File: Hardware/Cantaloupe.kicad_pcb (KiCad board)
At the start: 2 copper layers, 277.1 x 113 mm, 172 parts, among them J1 USB_C_Receptacle_PD, J2 Bat, J3 OLED, J4 USB_C_Receptacle_PD, J5 Bat, J6 OLED, SW1 MX, SW10 MX, SW11 MX, SW12 MX, SW13 MX, SW14 MX, SW15 MX, SW16 MX, SW17 MX, SW18 MX, SW19 MX, SW2 MX, SW20 MX, SW21 MX, SW22 MX, SW23 MX, SW24 MX, SW25 MX, SW26 MX, SW27 MX, SW28 MX, SW29 MX, SW3 MX, SW30 MX, SW31 5_Way_Tactile_Switch, SW32 Rotary_Encoder_Switch, SW33 5_Way_Tactile_Switch_R, SW34 Reset, SW35 MX, SW36 MX, SW37 MX, SW38 MX, SW39 MX, SW4 MX, SW40 MX, SW41 MX, SW42 MX, SW43 MX, SW44 MX, SW45 MX, SW46 MX, SW47 MX, SW48 MX, SW49 MX, SW5 MX, SW50 MX, SW51 MX, SW52 MX, SW53 MX, SW54 MX, SW55 MX, SW56 MX, SW57 MX, SW58 MX, SW59 MX, SW6 MX, SW60 MX, SW61 MX, SW62 MX, SW63 MX, SW65 MX, SW66 Rotary_Encoder_Switch, SW67 Reset, SW7 MX, SW8 MX, SW9 MX, U1 ProMicro, U2 ProMicro

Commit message: Proper case files and gerbers
Added an STL file for a rudimentary 3D-printed case for the Cantaloupe as well as DXF and Gerber files for a plate.
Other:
- board text added: "Cantaloupe Keyboard Left Hand Side V1.0 Designed By Aria"
- board text added: "Cantaloupe Keyboard Right Hand Side V1.0 Designed By Aria"
- board text removed: "Cantaloupe Keyboard Left Hand Side V2.1 Designed By Aria"
- board text removed: "Cantaloupe Keyboard Right Hand Side V2.1 Designed By Aria"

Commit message: Interconnect changed to C-168688
Changed interconnect footprint to USB C-168688 due to lack of widespread availability of previous part.
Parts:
- J1, J4: footprint Cantaloupe:USB-C-PowerOnly -> Cantaloupe:USB-C-C168688
- R1: value 4.7k -> 10k
- R2: renamed from R4; value 4.7k -> 10k
- moved J4 0.73 mm to (69.1, 113.6)
- moved J1 0.72 mm to (348.1, 113.6)
- renumbered SW32 to SW31, SW31 to SW32, SW34 to SW33, SW35 to SW34, SW36 to SW35, SW37 to SW36, SW38 to SW37, SW39 to SW38, SW40 to SW39, SW41 to SW40, SW42 to SW41, SW43 to SW42, SW44 to SW43, SW45 to SW44, SW46 to SW45, SW47 to SW46, SW48 to SW47, SW49 to SW48, SW50 to SW49, SW51 to SW50, SW52 to SW51, SW53 to SW52, SW58 to SW53, SW63 to SW58, SW65 to SW63, SW66 to SW64, SW33 to SW65, SW67 to SW66
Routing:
- net DATA_R: track 47.7 -> 50.3 mm
- net DATA: track 46.5 -> 49.1 mm
- net VCC: track 73.4 -> 72.3 mm
- net GND3: track 247.1 -> 246.0 mm
- net GND1: track 99.1 -> 98.1 mm
- net VDD: track 65.4 -> 66.4 mm

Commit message: Updated to V1.1
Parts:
- removed D63, D64, D65, D66, D67, D68, D69, D70: D, Diode_SMD:D_SOD-123
- removed H1, H10, H2, H3, H4, H5, H6, H7, H8, H9: MountingHole, MountingHole:MountingHole_2.2mm_M2_Pad
- removed H11 (x2), H12 (x2), H13 (x2), H14 (x2), H15 (x2): Breakaway, Cantaloupe:Breakaway_Tabs
- removed R1, R2: 10k, Resistor_SMD:R_0603_1608Metric_Pad1.05x0.95mm_HandSolder
- removed the REF** at (343.6, 94.9)
- removed the REF** at (327.6, 94.9)
- removed the REF** at (89.5, 94.9)
- removed the REF** at (73.5, 94.9)
- added J7: BAT_CON_TOG, Cantaloupe:Battery_Solder_Points, F.Cu at (309.2, 33.8)
- added J8: BAT_CON_R, Cantaloupe:Battery_Solder_Points, F.Cu at (77.6, 39.1)
- added J9: BAT_CON, Cantaloupe:Battery_Solder_Points, F.Cu at (334.6, 39.1)
- added REF**: MountingHole_2.2mm_M2_Pad, MountingHole:MountingHole_2.2mm_M2_Pad, F.Cu at (174.6, 60.3)
- added REF**: Breakaway_Tabs, Custom Parts:Breakaway_Tabs, F.Cu at (193.9, 127.0)
- added REF**: Breakaway_Tabs, Custom Parts:Breakaway_Tabs, F.Cu at (193.9, 88.9)
- added REF**: Breakaway_Tabs, Custom Parts:Breakaway_Tabs, F.Cu at (193.9, 69.8)
- added REF**: Breakaway_Tabs, Custom Parts:Breakaway_Tabs, F.Cu at (193.9, 108.0)
- added REF**: LiPo_501235, Custom Parts:LiPo_501235, F.Cu at (317.4, 92.9)
- added REF**: MountingHole_2.2mm_M2_Pad, MountingHole:MountingHole_2.2mm_M2_Pad, F.Cu at (330.4, 72.5)
- added REF**: MountingHole_2.2mm_M2_Pad, MountingHole:MountingHole_2.2mm_M2_Pad, F.Cu at (314.4, 72.5)
- added REF**: MountingHole_2.2mm_M2_Pad, MountingHole:MountingHole_2.2mm_M2_Pad, F.Cu at (309.4, 121.5)
- added REF**: MountingHole_2.2mm_M2_Pad, MountingHole:MountingHole_2.2mm_M2_Pad, F.Cu at (270.3, 112.7)
- added REF**: MountingHole_2.2mm_M2_Pad, MountingHole:MountingHole_2.2mm_M2_Pad, F.Cu at (289.4, 57.1)
- added REF**: MountingHole_2.2mm_M2_Pad, MountingHole:MountingHole_2.2mm_M2_Pad, F.Cu at (98.4, 57.1)
- added REF**: MountingHole_2.2mm_M2_Pad, MountingHole:MountingHole_2.2mm_M2_Pad, F.Cu at (213.2, 117.5)
- added REF**: MountingHole_2.2mm_M2_Pad, MountingHole:MountingHole_2.2mm_M2_Pad, F.Cu at (213.2, 60.3)
- added REF**: MountingHole_2.2mm_M2_Pad, MountingHole:MountingHole_2.2mm_M2_Pad, F.Cu at (117.5, 112.7)
- added REF**: MountingHole_2.2mm_M2_Pad, MountingHole:MountingHole_2.2mm_M2_Pad, F.Cu at (174.6, 117.5)
- added REF**: MountingHole_2.2mm_M2_Pad, MountingHole:MountingHole_2.2mm_M2_Pad, F.Cu at (78.4, 121.5)
- added REF**: MountingHole_2.2mm_M2_Pad, MountingHole:MountingHole_2.2mm_M2_Pad, F.Cu at (73.4, 72.3)
- added REF**: MountingHole_2.2mm_M2_Pad, MountingHole:MountingHole_2.2mm_M2_Pad, F.Cu at (57.4, 72.3)
- added REF**: LiPo_501235, Custom Parts:LiPo_501235, F.Cu at (70.4, 92.9)
- added REF**: Breakaway_Tabs, Custom Parts:Breakaway_Tabs, F.Cu at (193.9, 50.8)
- added SW67: BAT_TOG, Cantaloupe:Switch_MSK-22D18, F.Cu at (303.2, 35.1)
- added SW68: BAT_TOG_R, Cantaloupe:Switch_MSK-22D18, F.Cu at (84.6, 35.1)
- J1, J4: value USB_C_Receptacle_PD -> OLED; footprint Cantaloupe:USB-C-C168688 -> Cantaloupe:PinHeader_1x04_P2.54mm_Vertical_No_Silk; moved to F.Cu
- J2: value Bat -> Interconnect; footprint Cantaloupe:Battery_Solder_Points -> Cantaloupe:USB-C_C168688; moved to B.Cu
- J3: value OLED -> ICSP; footprint Cantaloupe:PinHeader_1x04_P2.54mm_Vertical_No_Silk -> Connector_PinHeader_2.54mm:PinHeader_2x03_P2.54mm_Vertical; moved to B.Cu
- J5: value Bat -> Interconnect_R; footprint Cantaloupe:Battery_Solder_Points -> Cantaloupe:USB-C_C168688; moved to B.Cu
- J6: value OLED -> ICSP_R; footprint Cantaloupe:PinHeader_1x04_P2.54mm_Vertical_No_Silk -> Connector_PinHeader_2.54mm:PinHeader_2x03_P2.54mm_Vertical; moved to B.Cu
- SW31, SW64: value Rotary_Encoder_Switch -> MX; footprint Rotary_Encoder:RotaryEncoder_Alps_EC11E-Switch_Vertical_H20mm -> Cantaloupe:CherryMX_Hotswap_SMK
- SW32: value 5_Way_Tactile_Switch -> Encoder; footprint Cantaloupe:5-way_Tactile_Switch -> Rotary_Encoder:RotaryEncoder_Alps_EC11E-Switch_Vertical_H20mm
- SW65: value 5_Way_Tactile_Switch_R -> Encoder_R; footprint Cantaloupe:5-way_Tactile_Switch -> Rotary_Encoder:RotaryEncoder_Alps_EC11E-Switch_Vertical_H20mm
- moved SW34 144.1 mm to (63.5, 120.3), turned to 30 degrees
- moved D32 143.2 mm to (70.3, 116.3), turned to 120 degrees
- moved SW35 134.2 mm to (73.0, 136.8), turned to 30 degrees
- moved D33 133.3 mm to (79.9, 132.8), turned to 120 degrees
- moved SW36 125.3 mm to (88.9, 49.2)
- moved SW38 125.3 mm to (88.9, 87.3)
- moved SW37 125.3 mm to (88.9, 68.3)
- moved D36 124.8 mm to (96.8, 87.3)
- moved D35 124.8 mm to (96.8, 68.3)
- moved D34 124.8 mm to (96.8, 49.2)
- moved SW63 105.1 mm to (184.2, 108.0), turned to 0 degrees
- moved SW64 103.6 mm to (184.2, 127.0), turned to 0 degrees
- moved D61 102.7 mm to (192.1, 108.0), turned to 90 degrees
- moved D62 98.5 mm to (192.1, 127.0), turned to 90 degrees
- moved D58 98.0 mm to (192.1, 50.8)
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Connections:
- D30 pad 1: ROW1 -> ROW4
- D32 pad 1: ROW1_R -> ROW4_R
- D33 pad 1: ROW2_R -> ROW5_R
- D34 pad 1: ROW3_R -> ROW1_R
- D35 pad 1: ROW4_R -> ROW2_R
- D36 pad 1: ROW5_R -> ROW3_R
- D37 pad 1: ROW1_R -> ROW4_R
- D38 pad 1: ROW2_R -> ROW5_R
- D39 pad 1: ROW3_R -> ROW1_R
- D40 pad 1: ROW4_R -> ROW2_R
- D41 pad 1: ROW5_R -> ROW3_R
- D42 pad 1: ROW1_R -> ROW4_R
- D43 pad 1: ROW2_R -> ROW5_R
- D44 pad 1: ROW3_R -> ROW1_R
- D45 pad 1: ROW4_R -> ROW2_R
- D46 pad 1: ROW5_R -> ROW3_R
- D47 pad 1: ROW1_R -> ROW4_R
- D48 pad 1: ROW2_R -> ROW1_R
- D49 pad 1: ROW3_R -> ROW2_R
- D50 pad 1: ROW4_R -> ROW3_R
- D51 pad 1: ROW1_R -> ROW4_R
- D52 pad 1: ROW2_R -> ROW5_R
- D53 pad 1: ROW3_R -> ROW1_R
- D54 pad 1: ROW4_R -> ROW2_R
- D55 pad 1: ROW5_R -> ROW3_R
- D56 pad 1: ROW1_R -> ROW4_R
- D57 pad 1: ROW2_R -> ROW5_R
- D58 pad 1: ROW3_R -> ROW1_R
- D59 pad 1: ROW4_R -> ROW2_R
- D60 pad 1: ROW5_R -> ROW3_R
- D61 pad 1: ROW1_R -> ROW4_R
- J3 pad 1: GND1 -> ROW4
- J3 pad 3: SCL -> ROW5
- J3 pad 4: SDA -> ROW3
- J6 pad 1: GND3 -> COL5_R
- J6 pad 3: SCL_R -> COL4_R
- J6 pad 4: SDA_R -> COL6_R
- SW24 pad 1: COL4 -> COL5
- SW29 pad 1: COL5 -> COL6
- SW30 pad 1: COL6 -> COL7
- SW30 pad 2: Net-(D31-Pad2) -> Net-(D30-Pad2)
- SW33 pad 2: GND2 -> GND1
- SW34 pad 1: COL1_R -> COL7_R
- SW35 pad 1: COL1_R -> COL7_R
- SW36 pad 1: COL1_R -> COL6_R
- SW37 pad 1: COL1_R -> COL6_R
- SW38 pad 1: COL1_R -> COL6_R
- SW39 pad 1: COL2_R -> COL6_R
- SW40 pad 1: COL2_R -> COL6_R
- SW41 pad 1: COL2_R -> COL5_R
- SW42 pad 1: COL2_R -> COL5_R
- SW43 pad 1: COL2_R -> COL5_R
- SW44 pad 1: COL3_R -> COL5_R
- SW45 pad 1: COL3_R -> COL5_R
- SW46 pad 1: COL3_R -> COL4_R
- SW47 pad 1: COL3_R -> COL4_R
- SW48 pad 1: COL3_R -> COL4_R
- SW50 pad 1: COL4_R -> COL3_R
- SW51 pad 1: COL4_R -> COL3_R
- SW52 pad 1: COL4_R -> COL3_R
- SW53 pad 1: COL4_R -> COL3_R
- SW53 pad 2: Net-(D55-Pad2) -> Net-(D51-Pad2)
- SW54 pad 1: COL5_R -> COL3_R
- SW54 pad 2: Net-(D51-Pad2) -> Net-(D52-Pad2)
- SW55 pad 1: COL5_R -> COL2_R
- SW55 pad 2: Net-(D52-Pad2) -> Net-(D53-Pad2)
- SW56 pad 1: COL5_R -> COL2_R
- SW56 pad 2: Net-(D53-Pad2) -> Net-(D54-Pad2)
- SW57 pad 1: COL5_R -> COL2_R
- SW57 pad 2: Net-(D54-Pad2) -> Net-(D55-Pad2)
- SW58 pad 1: COL5_R -> COL2_R
- SW58 pad 2: Net-(D60-Pad2) -> Net-(D56-Pad2)
- SW59 pad 1: COL6_R -> COL2_R
- SW59 pad 2: Net-(D56-Pad2) -> Net-(D57-Pad2)
- SW60 pad 1: COL6_R -> COL1_R
- SW60 pad 2: Net-(D57-Pad2) -> Net-(D58-Pad2)
- SW61 pad 1: COL6_R -> COL1_R
- SW61 pad 2: Net-(D58-Pad2) -> Net-(D59-Pad2)
- SW62 pad 1: COL6_R -> COL1_R
- SW62 pad 2: Net-(D59-Pad2) -> Net-(D60-Pad2)
- SW63 pad 1: COL6_R -> COL1_R
- SW63 pad 2: Net-(D62-Pad2) -> Net-(D61-Pad2)
- U1 pad 1: ROTA -> ROW1
- U1 pad 10: DATA -> COL4
- U1 pad 11: COL4 -> COL5
- U1 pad 12: COL5 -> COL6
- U1 pad 13: ROW1 -> ROW2
- U1 pad 14: ROW2 -> ROW3
- U1 pad 15: COL6 -> ROW4
- U1 pad 16: ROW3 -> ROW5
- U1 pad 17: ROW4 -> ROT_B
- U1 pad 18: ROW5 -> ROT_A
- U1 pad 2: ROTB -> DATA
- U1 pad 24: Net-(J2-Pad2) -> Net-(J9-Pad2)
- U1 pad 3: GND2 -> Net-(U1-Pad3)
- U1 pad 4: GND2 -> Net-(U1-Pad4)
- U2 pad 1: ROW5_R -> COL7_R
- U2 pad 10: DATA_R -> ROW4_R
- U2 pad 11: Net-(U2-Pad11) -> ROW3_R
- U2 pad 12: COL7_R -> ROW2_R
- U2 pad 13: ROTA_R -> Net-(U2-Pad13)
- U2 pad 14: ROTB_R -> COL6_R
- U2 pad 15: COL6_R -> COL5_R
- U2 pad 16: COL5_R -> COL4_R
- U2 pad 17: COL4_R -> COL3_R
- U2 pad 18: COL3_R -> COL2_R
- U2 pad 19: COL2_R -> COL1_R
- U2 pad 2: ROW4_R -> DATA_R
- U2 pad 20: COL1_R -> ROW1_R
- U2 pad 24: Net-(J5-Pad2) -> RAW_R
- U2 pad 7: ROW3_R -> ROT_A_R
- U2 pad 8: ROW2_R -> ROT_B_R
- U2 pad 9: ROW1_R -> ROW5_R
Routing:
- net GND2: track 145.9 -> 0.00 mm, vias 3 -> 0
- net ROT_A_R: track 0.00 -> 104.4 mm
- net ROT_B: track 0.00 -> 103.3 mm
- net ROTA: track 99.2 -> 0.00 mm
- net ROT_A: track 0.00 -> 98.9 mm
- net ROT_B_R: track 0.00 -> 96.2 mm
- net ROTB: track 87.4 -> 0.00 mm
- net GND3: track 246.0 -> 169.3 mm, vias 2 -> 0
- net COL7_R: track 90.3 -> 166.1 mm, vias 2 -> 0
- net ROTB_R: track 75.2 -> 0.00 mm, vias 1 -> 0
- net ROW1_R: track 217.8 -> 148.8 mm, vias 3 -> 0
- net ROTA_R: track 65.0 -> 0.00 mm, vias 1 -> 0
- net GND1: track 98.1 -> 159.8 mm
- net ROW4: track 188.0 -> 247.9 mm, vias 0 -> 3
- net ROW1: track 198.0 -> 138.6 mm, vias 3 -> 0
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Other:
- board size 277.1 x 113 mm -> 284.6 x 117 mm
- net class Battery added: clearance 0.2, trace_width 1, via_dia 0.7, via_drill 0.35
- board text added: "Cantaloupe Left V1.1 Aria"
- board text added: "Cantaloupe Right V1.1 Aria"
- board text added: "JLCJLCJLCJLC"
- board text added: "OLED"
- board text removed: "Cantaloupe Keyboard Left Hand Side V1.0 Designed By Aria"
- board text removed: "Cantaloupe Keyboard Right Hand Side V1.0 Designed By Aria"
- board text removed: "JLCJLCJLC"

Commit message: Increased gap between halves
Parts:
- removed the REF** at (174.6, 60.3)
- removed the REF** at (193.9, 127.0)
- removed the REF** at (193.9, 88.9)
- removed the REF** at (193.9, 69.8)
- removed the REF** at (193.9, 108.0)
- removed the REF** at (309.4, 121.5)
- removed the REF** at (270.3, 112.7)
- removed the REF** at (289.4, 57.1)
- removed the REF** at (98.4, 57.1)
- removed the REF** at (213.2, 117.5)
- removed the REF** at (213.2, 60.3)
- removed the REF** at (117.5, 112.7)
- removed the REF** at (174.6, 117.5)
- removed the REF** at (193.9, 50.8)
- added REF**: Breakaway_Tabs, Custom Parts:Breakaway_Tabs, F.Cu at (196.8, 88.8)
- added REF**: Breakaway_Tabs, Custom Parts:Breakaway_Tabs, F.Cu at (193.7, 69.8)
- added REF**: MountingHole_2.2mm_M2_Pad, MountingHole:MountingHole_2.2mm_M2_Pad, F.Cu at (174.6, 60.3)
- added REF**: MountingHole_2.2mm_M2_Pad, MountingHole:MountingHole_2.2mm_M2_Pad, F.Cu at (98.4, 57.1)
- added REF**: MountingHole_2.2mm_M2_Pad, MountingHole:MountingHole_2.2mm_M2_Pad, F.Cu at (117.5, 112.6)
- added REF**: MountingHole_2.2mm_M2_Pad, MountingHole:MountingHole_2.2mm_M2_Pad, F.Cu at (174.6, 117.4)
- added REF**: Breakaway_Tabs, Custom Parts:Breakaway_Tabs, F.Cu at (193.7, 107.9)
- added REF**: MountingHole_2.2mm_M2_Pad, MountingHole:MountingHole_2.2mm_M2_Pad, F.Cu at (312.2, 121.5)
- added REF**: MountingHole_2.2mm_M2_Pad, MountingHole:MountingHole_2.2mm_M2_Pad, F.Cu at (273.1, 112.6)
- added REF**: MountingHole_2.2mm_M2_Pad, MountingHole:MountingHole_2.2mm_M2_Pad, F.Cu at (292.1, 57.1)
- added REF**: MountingHole_2.2mm_M2_Pad, MountingHole:MountingHole_2.2mm_M2_Pad, F.Cu at (215.9, 117.4)
- added REF**: MountingHole_2.2mm_M2_Pad, MountingHole:MountingHole_2.2mm_M2_Pad, F.Cu at (215.9, 60.3)
- added REF**: Breakaway_Tabs, Custom Parts:Breakaway_Tabs, F.Cu at (196.8, 126.9)
- added REF**: Breakaway_Tabs, Custom Parts:Breakaway_Tabs, F.Cu at (196.8, 107.9)
- added REF**: Breakaway_Tabs, Custom Parts:Breakaway_Tabs, F.Cu at (193.7, 126.9)
- added REF**: Breakaway_Tabs, Custom Parts:Breakaway_Tabs, F.Cu at (193.7, 88.8)
- added REF**: Breakaway_Tabs, Custom Parts:Breakaway_Tabs, F.Cu at (196.8, 50.7)
- added REF**: Breakaway_Tabs, Custom Parts:Breakaway_Tabs, F.Cu at (193.7, 50.7)
- added REF**: Breakaway_Tabs, Custom Parts:Breakaway_Tabs, F.Cu at (196.8, 69.8)
- moved J3 2.74 mm to (337.0, 104.1)
- moved D1 2.74 mm to (214.3, 50.7)
- moved D10 2.74 mm to (233.4, 126.9)
- moved D2 2.74 mm to (214.3, 69.8)
- moved D20 2.74 mm to (290.5, 46.0)
- moved D21 2.74 mm to (290.5, 65.0)
- moved D22 2.74 mm to (290.5, 84.1)
- moved D23 2.74 mm to (290.5, 103.1)
- moved D24 2.74 mm to (284.2, 126.9)
- moved D25 2.74 mm to (309.6, 49.1)
- moved D26 2.74 mm to (309.6, 68.2)
- moved D27 2.74 mm to (309.6, 87.2)
- moved D28 2.74 mm to (309.6, 106.3)
- moved D29 2.74 mm to (305.0, 130.9)
- moved D3 2.74 mm to (214.3, 88.8)
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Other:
- board size 284.6 x 117 mm -> 287.3 x 117 mm

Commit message: Better photo, reorganized footprints, minor fixes to circuit
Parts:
- removed the D32 at (70.3, 116.2)
- removed the D33 at (79.9, 132.7)
- removed the D38 at (100.6, 127.3)
- removed the SW30 at (327.1, 120.2)
- removed the SW34 at (63.5, 120.2)
- added D56: D, Diode_SMD:D_SOD-123, B.Cu at (80.6, 134.0)
- added D57: D, Diode_SMD:D_SOD-123, B.Cu at (101.1, 128.5)
- added D62: D, Diode_SMD:D_SOD-123, B.Cu at (71.1, 117.5)
- added SW32: 5_Way, Cantaloupe:Switch_5-way-tactile, F.Cu at (327.1, 120.2)
- added SW66: 5_Way_R, Cantaloupe:Switch_5-way-tactile, F.Cu at (63.5, 120.2)
- SW1, SW23, SW29, SW42, SW64: footprint Cantaloupe:CherryMX_Hotswap_SMK -> Cantaloupe:MX-1U-Hotswap
- SW10: renamed from SW17; footprint Cantaloupe:CherryMX_Hotswap_SMK -> Cantaloupe:MX-1U-Hotswap
- SW11: renamed from SW21; footprint Cantaloupe:CherryMX_Hotswap_SMK -> Cantaloupe:MX-1U-Hotswap
- SW12: renamed from SW26; footprint Cantaloupe:CherryMX_Hotswap_SMK -> Cantaloupe:MX-1U-Hotswap
- SW13: renamed from SW3; footprint Cantaloupe:CherryMX_Hotswap_SMK -> Cantaloupe:MX-1U-Hotswap
- SW14: renamed from SW8; footprint Cantaloupe:CherryMX_Hotswap_SMK -> Cantaloupe:MX-1U-Hotswap
- SW15: renamed from SW13; footprint Cantaloupe:CherryMX_Hotswap_SMK -> Cantaloupe:MX-1U-Hotswap
- SW16: renamed from SW18; footprint Cantaloupe:CherryMX_Hotswap_SMK -> Cantaloupe:MX-1U-Hotswap
- SW17: renamed from SW22; footprint Cantaloupe:CherryMX_Hotswap_SMK -> Cantaloupe:MX-1U-Hotswap
- SW18: renamed from SW27; footprint Cantaloupe:CherryMX_Hotswap_SMK -> Cantaloupe:MX-1U-Hotswap
- SW19: renamed from SW4; footprint Cantaloupe:CherryMX_Hotswap_SMK -> Cantaloupe:MX-1U-Hotswap
- SW2: renamed from SW6; footprint Cantaloupe:CherryMX_Hotswap_SMK -> Cantaloupe:MX-1U-Hotswap
- SW20: renamed from SW9; footprint Cantaloupe:CherryMX_Hotswap_SMK -> Cantaloupe:MX-1U-Hotswap
- SW21: renamed from SW14; footprint Cantaloupe:CherryMX_Hotswap_SMK -> Cantaloupe:MX-1U-Hotswap
- SW22: renamed from SW19; footprint Cantaloupe:CherryMX_Hotswap_SMK -> Cantaloupe:MX-1U-Hotswap
- SW24: renamed from SW28; footprint Cantaloupe:CherryMX_Hotswap_SMK -> Cantaloupe:MX-1U-Hotswap
- SW25: renamed from SW5; footprint Cantaloupe:CherryMX_Hotswap_SMK -> Cantaloupe:MX-1U-Hotswap
- SW26: renamed from SW10; footprint Cantaloupe:CherryMX_Hotswap_SMK -> Cantaloupe:MX-1U-Hotswap
- SW27: renamed from SW15; footprint Cantaloupe:CherryMX_Hotswap_SMK -> Cantaloupe:MX-1U-Hotswap
- SW28: renamed from SW24; footprint Cantaloupe:CherryMX_Hotswap_SMK -> Cantaloupe:MX-1U-Hotswap
- SW3: renamed from SW11; footprint Cantaloupe:CherryMX_Hotswap_SMK -> Cantaloupe:MX-1U-Hotswap
- SW30: renamed from SW31; footprint Cantaloupe:CherryMX_Hotswap_SMK -> Cantaloupe:MX-1U-Hotswap
- SW35: renamed from SW36; footprint Cantaloupe:CherryMX_Hotswap_SMK -> Cantaloupe:MX-1U-Hotswap
- SW36: renamed from SW41; footprint Cantaloupe:CherryMX_Hotswap_SMK -> Cantaloupe:MX-1U-Hotswap
- SW37: renamed from SW46; footprint Cantaloupe:CherryMX_Hotswap_SMK -> Cantaloupe:MX-1U-Hotswap
- SW38: renamed from SW50; footprint Cantaloupe:CherryMX_Hotswap_SMK -> Cantaloupe:MX-1U-Hotswap
- SW39: renamed from SW55; footprint Cantaloupe:CherryMX_Hotswap_SMK -> Cantaloupe:MX-1U-Hotswap
- SW4: renamed from SW16; footprint Cantaloupe:CherryMX_Hotswap_SMK -> Cantaloupe:MX-1U-Hotswap
- SW40: renamed from SW60; footprint Cantaloupe:CherryMX_Hotswap_SMK -> Cantaloupe:MX-1U-Hotswap
- SW41: renamed from SW37; footprint Cantaloupe:CherryMX_Hotswap_SMK -> Cantaloupe:MX-1U-Hotswap
- SW43: renamed from SW47; footprint Cantaloupe:CherryMX_Hotswap_SMK -> Cantaloupe:MX-1U-Hotswap
- SW44: renamed from SW51; footprint Cantaloupe:CherryMX_Hotswap_SMK -> Cantaloupe:MX-1U-Hotswap
- SW45: renamed from SW56; footprint Cantaloupe:CherryMX_Hotswap_SMK -> Cantaloupe:MX-1U-Hotswap
- SW46: renamed from SW61; footprint Cantaloupe:CherryMX_Hotswap_SMK -> Cantaloupe:MX-1U-Hotswap
- SW47: renamed from SW38; footprint Cantaloupe:CherryMX_Hotswap_SMK -> Cantaloupe:MX-1U-Hotswap
- SW48: renamed from SW43; footprint Cantaloupe:CherryMX_Hotswap_SMK -> Cantaloupe:MX-1U-Hotswap
- SW49: renamed from SW48; footprint Cantaloupe:CherryMX_Hotswap_SMK -> Cantaloupe:MX-1U-Hotswap
- SW5: renamed from SW20; footprint Cantaloupe:CherryMX_Hotswap_SMK -> Cantaloupe:MX-1U-Hotswap
- SW50: renamed from SW52; footprint Cantaloupe:CherryMX_Hotswap_SMK -> Cantaloupe:MX-1U-Hotswap
- SW51: renamed from SW57; footprint Cantaloupe:CherryMX_Hotswap_SMK -> Cantaloupe:MX-1U-Hotswap
- SW52: renamed from SW62; footprint Cantaloupe:CherryMX_Hotswap_SMK -> Cantaloupe:MX-1U-Hotswap
- SW53: renamed from SW39; footprint Cantaloupe:CherryMX_Hotswap_SMK -> Cantaloupe:MX-1U-Hotswap
- SW54: renamed from SW44; footprint Cantaloupe:CherryMX_Hotswap_SMK -> Cantaloupe:MX-1U-Hotswap
- SW55: renamed from SW49; footprint Cantaloupe:CherryMX_Hotswap_SMK -> Cantaloupe:MX-1U-Hotswap
- SW56: renamed from SW53; footprint Cantaloupe:CherryMX_Hotswap_SMK -> Cantaloupe:MX-1U-Hotswap
- SW57: renamed from SW58; footprint Cantaloupe:CherryMX_Hotswap_SMK -> Cantaloupe:MX-1U-Hotswap
- SW58: renamed from SW63; footprint Cantaloupe:CherryMX_Hotswap_SMK -> Cantaloupe:MX-1U-Hotswap
- SW59: renamed from SW35; footprint Cantaloupe:CherryMX_Hotswap_SMK -> Cantaloupe:MX-1U-Hotswap
- SW6: renamed from SW25; footprint Cantaloupe:CherryMX_Hotswap_SMK -> Cantaloupe:MX-1U-Hotswap
- SW60: renamed from SW40; footprint Cantaloupe:CherryMX_Hotswap_SMK -> Cantaloupe:MX-1U-Hotswap
- SW61: renamed from SW45; footprint Cantaloupe:CherryMX_Hotswap_SMK -> Cantaloupe:MX-1U-Hotswap
- SW62: renamed from SW54; footprint Cantaloupe:CherryMX_Hotswap_SMK -> Cantaloupe:MX-1U-Hotswap
- SW63: renamed from SW59; footprint Cantaloupe:CherryMX_Hotswap_SMK -> Cantaloupe:MX-1U-Hotswap
- SW7: renamed from SW2; footprint Cantaloupe:CherryMX_Hotswap_SMK -> Cantaloupe:MX-1U-Hotswap
- SW8: renamed from SW7; footprint Cantaloupe:CherryMX_Hotswap_SMK -> Cantaloupe:MX-1U-Hotswap
- SW9: renamed from SW12; footprint Cantaloupe:CherryMX_Hotswap_SMK -> Cantaloupe:MX-1U-Hotswap
- moved D30 20.6 mm to (323.7, 142.0)
- moved D31 17.6 mm to (333.2, 125.5), turned to 240 degrees
- moved G1 2.47 mm to (261.1, 119.8)
- moved D29 1.72 mm to (304.7, 132.6)
- moved D1 1.50 mm to (214.3, 52.2)
- moved D10 1.50 mm to (271.5, 62.6)
- moved D11 1.50 mm to (290.5, 66.5)
- moved D12 1.50 mm to (309.6, 69.7)
- moved D13 1.50 mm to (214.3, 90.3)
- moved D14 1.50 mm to (233.4, 90.3)
- moved D15 1.50 mm to (252.4, 85.6)
- moved D16 1.50 mm to (271.5, 81.6)
- moved D17 1.50 mm to (290.5, 85.6)
- moved D18 1.50 mm to (309.6, 88.7)
- moved D19 1.50 mm to (214.3, 109.4)
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- renumbered D17 to D10, D21 to D11, D26 to D12, D3 to D13, D8 to D14, D13 to D15, D18 to D16, D22 to D17, D27 to D18, D4 to D19, D6 to D2, D9 to D20, D14 to D21, D19 to D22, D28 to D24, D5 to D25, D10 to D26, D15 to D27, D24 to D28, D11 to D3, D34 to D32, D39 to D33, D44 to D34, D48 to D35, D53 to D36, D58 to D37, D35 to D38, D40 to D39, D16 to D4, D45 to D40, D49 to D41, D54 to D42, D59 to D43, D36 to D44, D41 to D45, D50 to D47, D55 to D48, D60 to D49, D20 to D5, D37 to D50, D42 to D51, D47 to D52, D51 to D53, D56 to D54, D61 to D55, D43 to D58, D52 to D59, D25 to D6, D57 to D60, D62 to D61, D2 to D7, D7 to D8, D12 to D9, J9 to J1, J1 to J2, J2 to J3, J3 to J4, J7 to J5, J4 to J6, J5 to J7, J6 to J8, J8 to J9, SW33 to SW31, SW67 to SW33, SW32 to SW34, SW66 to SW65, SW65 to SW67
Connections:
- D1 pad 1: ROW1 -> ROW0
- D10 pad 1: ROW2 -> ROW1
- D11 pad 1: ROW2 -> ROW1
- D12 pad 1: ROW2 -> ROW1
- D13 pad 1: ROW3 -> ROW2
- D14 pad 1: ROW3 -> ROW2
- D15 pad 1: ROW3 -> ROW2
- D16 pad 1: ROW3 -> ROW2
- D17 pad 1: ROW3 -> ROW2
- D18 pad 1: ROW3 -> ROW2
- D19 pad 1: ROW4 -> ROW3
- D2 pad 1: ROW1 -> ROW0
- D20 pad 1: ROW4 -> ROW3
- D21 pad 1: ROW4 -> ROW3
- D22 pad 1: ROW4 -> ROW3
- D23 pad 1: ROW4 -> ROW3
- D24 pad 1: ROW4 -> ROW3
- D25 pad 1: ROW5 -> ROW4
- D26 pad 1: ROW5 -> ROW4
- D27 pad 1: ROW5 -> ROW4
- D28 pad 1: ROW5 -> ROW4
- D29 pad 1: ROW5 -> ROW4
- D3 pad 1: ROW1 -> ROW0
- D31 pad 1: ROW5 -> Net-(D31-Pad1)
- D31 pad 2: Net-(D31-Pad2) -> PERIPH
- D32 pad 1: ROW1_R -> ROW0_R
- D33 pad 1: ROW1_R -> ROW0_R
- D34 pad 1: ROW1_R -> ROW0_R
- D35 pad 1: ROW1_R -> ROW0_R
- D36 pad 1: ROW1_R -> ROW0_R
- D37 pad 1: ROW1_R -> ROW0_R
- D38 pad 1: ROW2_R -> ROW1_R
- D39 pad 1: ROW2_R -> ROW1_R
- D4 pad 1: ROW1 -> ROW0
- D40 pad 1: ROW2_R -> ROW1_R
- D41 pad 1: ROW2_R -> ROW1_R
- D42 pad 1: ROW2_R -> ROW1_R
- D43 pad 1: ROW2_R -> ROW1_R
- D44 pad 1: ROW3_R -> ROW2_R
- D45 pad 1: ROW3_R -> ROW2_R
- D46 pad 1: ROW3_R -> ROW2_R
- D47 pad 1: ROW3_R -> ROW2_R
- D48 pad 1: ROW3_R -> ROW2_R
- D49 pad 1: ROW3_R -> ROW2_R
- D5 pad 1: ROW1 -> ROW0
- D50 pad 1: ROW4_R -> ROW3_R
- D51 pad 1: ROW4_R -> ROW3_R
- D52 pad 1: ROW4_R -> ROW3_R
- D53 pad 1: ROW4_R -> ROW3_R
- D54 pad 1: ROW4_R -> ROW3_R
- D55 pad 1: ROW4_R -> ROW3_R
- D58 pad 1: ROW5_R -> ROW4_R
- D59 pad 1: ROW5_R -> ROW4_R
- D6 pad 1: ROW1 -> ROW0
- D60 pad 1: ROW5_R -> ROW4_R
- D61 pad 1: ROW5_R -> ROW4_R
- D7 pad 1: ROW2 -> ROW1
- D8 pad 1: ROW2 -> ROW1
- D9 pad 1: ROW2 -> ROW1
- J4 pad 1: ROW4 -> ROW3
- J4 pad 3: ROW5 -> ROW4
- J4 pad 4: ROW3 -> ROW2
- J8 pad 1: COL5_R -> COL4_R
- J8 pad 3: COL4_R -> COL3_R
- J8 pad 4: COL6_R -> COL5_R
- SW1 pad 1: COL1 -> COL0
- SW10 pad 1: COL4 -> COL3
- SW11 pad 1: COL5 -> COL4
- SW12 pad 1: COL6 -> COL5
- SW13 pad 1: COL1 -> COL0
- SW14 pad 1: COL2 -> COL1
- SW15 pad 1: COL3 -> COL2
- SW16 pad 1: COL4 -> COL3
- SW17 pad 1: COL5 -> COL4
- SW18 pad 1: COL6 -> COL5
- SW19 pad 1: COL1 -> COL0
- SW2 pad 1: COL2 -> COL1
- SW20 pad 1: COL2 -> COL1
- SW21 pad 1: COL3 -> COL2
- SW22 pad 1: COL4 -> COL3
- SW23 pad 1: COL5 -> COL4
- SW24 pad 1: COL6 -> COL5
- SW25 pad 1: COL1 -> COL0
- SW26 pad 1: COL2 -> COL1
- SW27 pad 1: COL3 -> COL2
- SW28 pad 1: COL5 -> COL3
- SW29 pad 1: COL6 -> COL4
- SW3 pad 1: COL3 -> COL2
- SW30 pad 1: COL7 -> COL5
- SW30 pad 2: Net-(D31-Pad2) -> Net-(D30-Pad2)
- SW34 pad S1: Net-(D30-Pad2) -> Net-(D31-Pad1)
- SW34 pad S2: COL7 -> PERIPH
- SW35 pad 1: COL6_R -> COL5_R
- SW36 pad 1: COL5_R -> COL4_R
- SW37 pad 1: COL4_R -> COL3_R
- SW38 pad 1: COL3_R -> COL2_R
- SW39 pad 1: COL2_R -> COL1_R
- SW4 pad 1: COL4 -> COL3
- SW40 pad 1: COL1_R -> COL0_R
- SW41 pad 1: COL6_R -> COL5_R
- SW42 pad 1: COL5_R -> COL4_R
- SW43 pad 1: COL4_R -> COL3_R
- SW44 pad 1: COL3_R -> COL2_R
- SW45 pad 1: COL2_R -> COL1_R
- SW46 pad 1: COL1_R -> COL0_R
- SW47 pad 1: COL6_R -> COL5_R
- SW48 pad 1: COL5_R -> COL4_R
- SW49 pad 1: COL4_R -> COL3_R
- SW5 pad 1: COL5 -> COL4
- SW50 pad 1: COL3_R -> COL2_R
- SW51 pad 1: COL2_R -> COL1_R
- SW52 pad 1: COL1_R -> COL0_R
- SW53 pad 1: COL6_R -> COL5_R
- SW54 pad 1: COL5_R -> COL4_R
- SW55 pad 1: COL4_R -> COL3_R
- SW56 pad 1: COL3_R -> COL2_R
- SW57 pad 1: COL2_R -> COL1_R
- SW58 pad 1: COL1_R -> COL0_R
- SW59 pad 1: COL7_R -> COL5_R
- SW6 pad 1: COL6 -> COL5
- SW60 pad 1: COL6_R -> COL4_R
- SW61 pad 1: COL5_R -> COL3_R
- SW62 pad 1: COL3_R -> COL2_R
- SW63 pad 1: COL2_R -> COL1_R
- SW64 pad 1: COL1_R -> COL0_R
- SW67 pad S2: COL7_R -> PERIPH_R
- SW7 pad 1: COL1 -> COL0
- SW8 pad 1: COL2 -> COL1
- SW9 pad 1: COL3 -> COL2
- U1 pad 1: ROW1 -> ROW0
- U1 pad 10: COL4 -> COL3
- U1 pad 11: COL5 -> COL4
- U1 pad 12: COL6 -> COL5
- U1 pad 13: ROW2 -> ROW1
- U1 pad 14: ROW3 -> ROW2
- U1 pad 15: ROW4 -> ROW3
- U1 pad 16: ROW5 -> ROW4
- U1 pad 19: COL7 -> PERIPH
- U1 pad 7: COL1 -> COL0
- U1 pad 8: COL2 -> COL1
- U1 pad 9: COL3 -> COL2
- U2 pad 1: COL7_R -> PERIPH_R
- U2 pad 10: ROW4_R -> ROW3_R
- U2 pad 11: ROW3_R -> ROW2_R
- U2 pad 12: ROW2_R -> ROW1_R
- U2 pad 14: COL6_R -> COL5_R
- U2 pad 15: COL5_R -> COL4_R
- U2 pad 16: COL4_R -> COL3_R
- U2 pad 17: COL3_R -> COL2_R
- U2 pad 18: COL2_R -> COL1_R
- U2 pad 19: COL1_R -> COL0_R
- U2 pad 20: ROW1_R -> ROW0_R
- U2 pad 9: ROW5_R -> ROW4_R
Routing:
- net ROW5: track 264.7 -> 0.00 mm, vias 1 -> 0
- net ROW0_R: track 0.00 -> 231.9 mm, vias 0 -> 3
- net ROW5_R: track 229.8 -> 0.00 mm
- net COL6_R: track 215.3 -> 0.00 mm
- net COL0: track 0.00 -> 214.6 mm, vias 0 -> 5
- net ROW0: track 0.00 -> 206.5 mm, vias 0 -> 1
- net COL0_R: track 0.00 -> 201.8 mm, vias 0 -> 5
- net COL6: track 196.8 -> 0.00 mm
- net COL7_R: track 166.1 -> 0.00 mm
- net COL7: track 155.1 -> 0.00 mm, vias 1 -> 0
- net PERIPH_R: track 0.00 -> 124.5 mm
- net PERIPH: track 0.00 -> 115.4 mm
- net COL2_R: track 260.9 -> 164.6 mm, vias 0 -> 5
- net COL5_R: track 255.9 -> 164.3 mm, vias 1 -> 5
- net COL2: track 268.0 -> 180.2 mm, vias 0 -> 5
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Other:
- board text added: "Cantaloupe V1.1 Aria"
- board text removed: "Cantaloupe Left V1.1 Aria"
- board text removed: "Cantaloupe Right V1.1 Aria"

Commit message: Minor fix to position of RHS OLED
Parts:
- moved REF** 0.16 mm to (73.4, 72.4)
- moved REF** 0.16 mm to (57.4, 72.4)
- moved J6 0.07 mm to (65.4, 71.9)

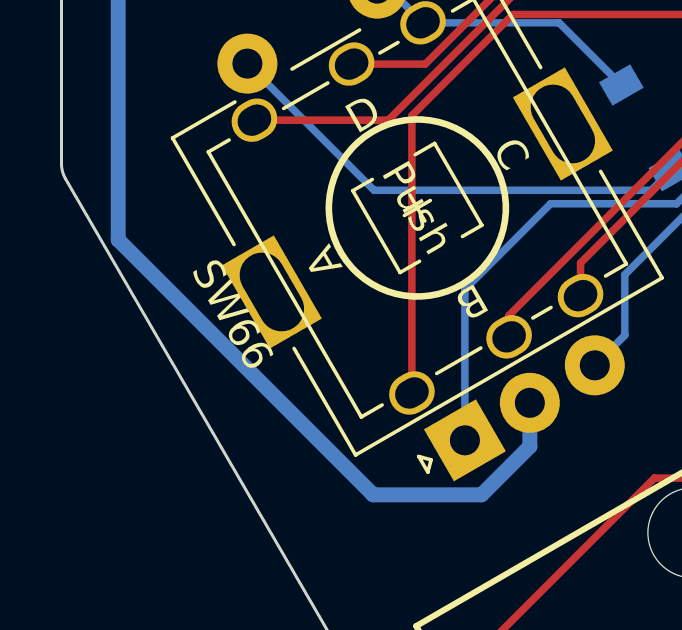
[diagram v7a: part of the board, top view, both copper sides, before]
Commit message: Fixed minor silk error
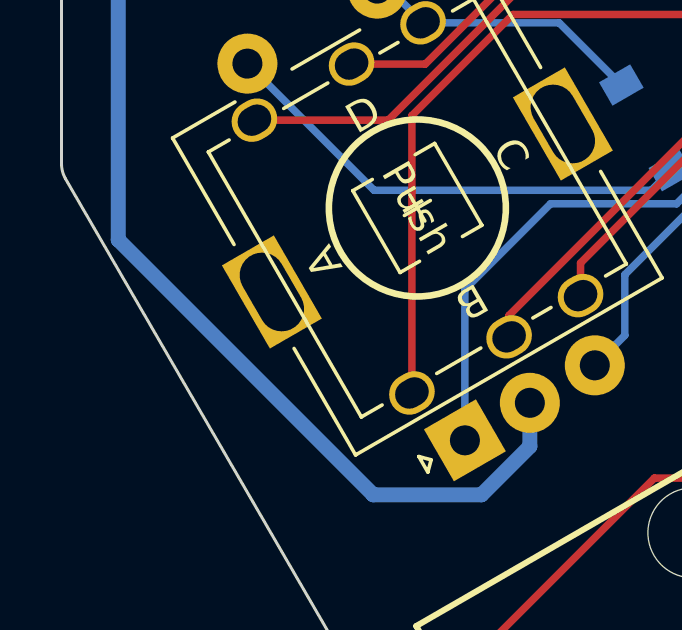
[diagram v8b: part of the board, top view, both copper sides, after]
